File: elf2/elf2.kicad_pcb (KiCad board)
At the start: 4 copper layers, 49.8 x 41.9 mm, 44 parts, among them J1 USB_B, J2 USB_Blaster, J3 JTAGEN, J4 PMOD_I2C, J5 PMOD_6P, J6 PMOD_6P2, J7 SWD, J8 ADC_LVDS, SW1 RESET, U1 EF2M45LG48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

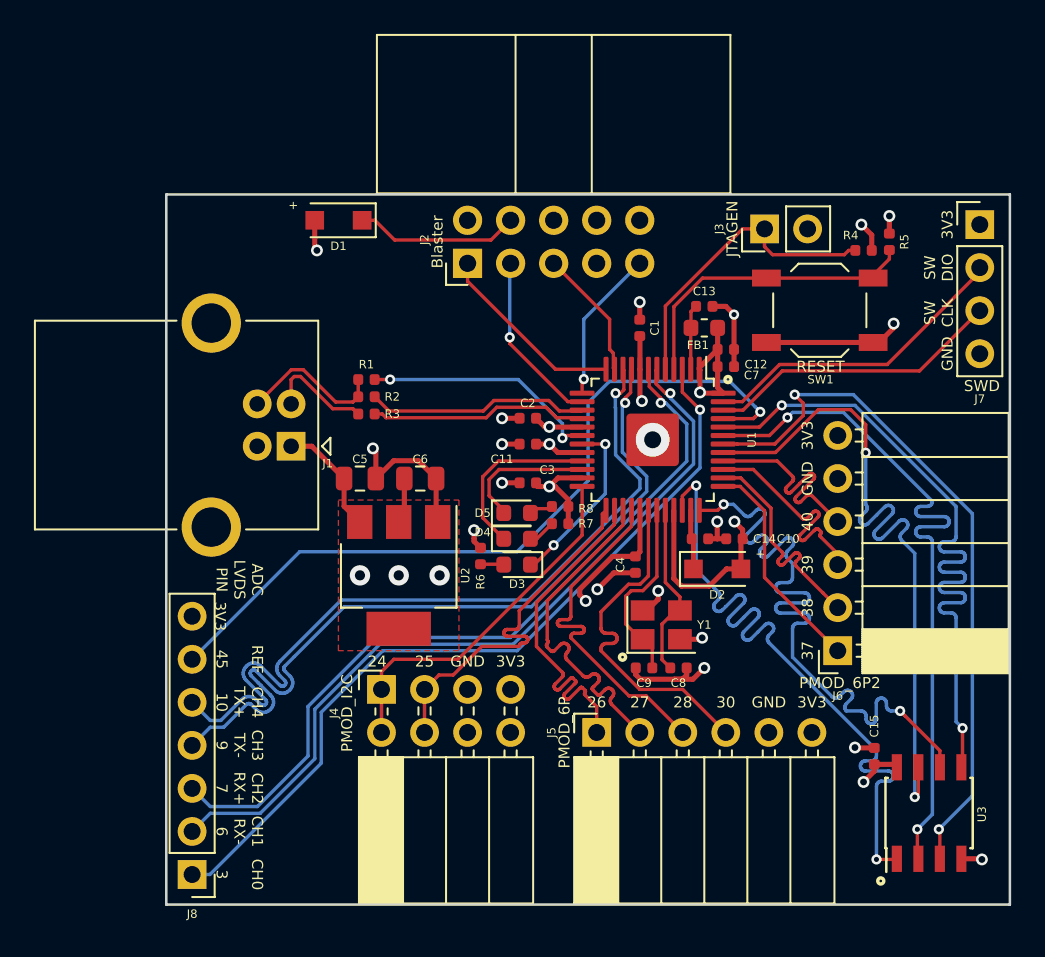
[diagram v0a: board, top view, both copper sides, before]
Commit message: update elf2 to v2
Signed-off-by: Icenowy Zheng <icenowy@aosc.io>
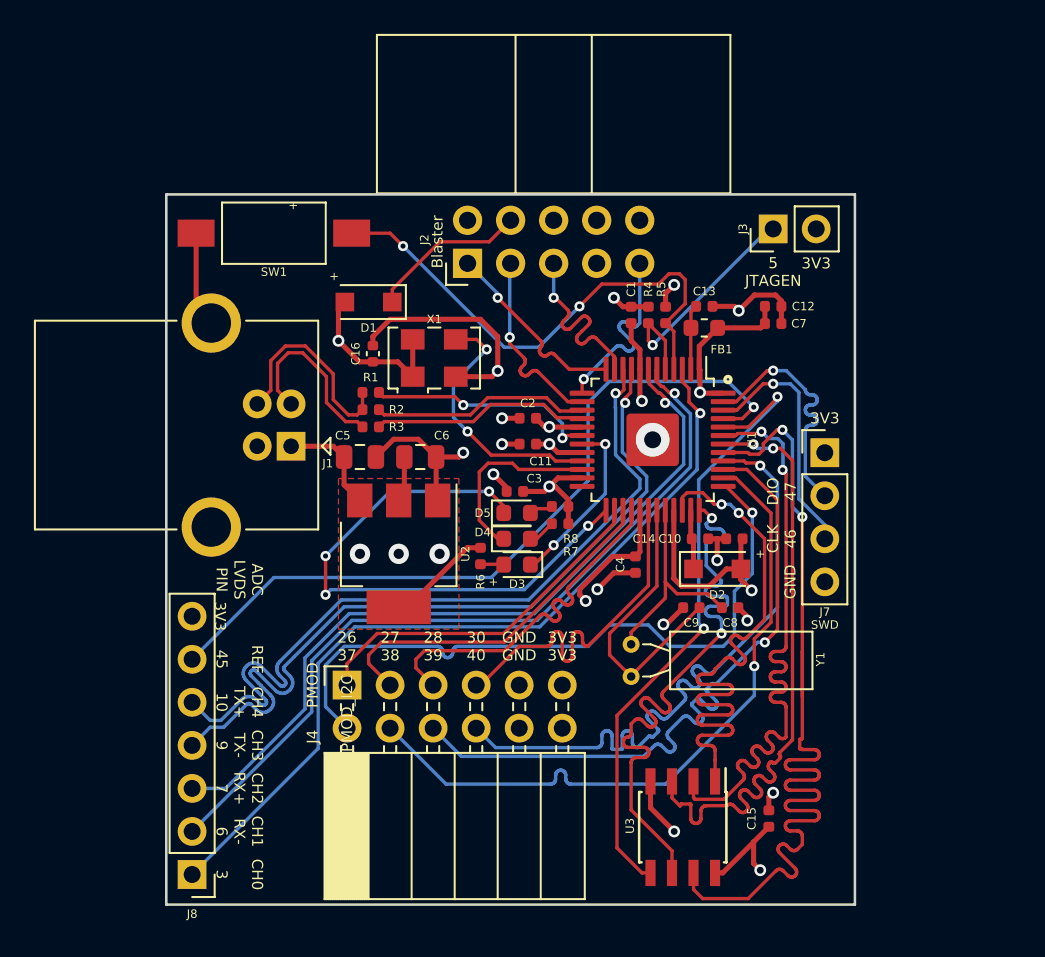
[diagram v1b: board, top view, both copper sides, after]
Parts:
- removed J5: PMOD_6P, Connector_PinSocket_2.54mm:PinSocket_1x06_P2.54mm_Horizontal
- removed J6: PMOD_6P2, Connector_PinSocket_2.54mm:PinSocket_1x06_P2.54mm_Horizontal
- removed the REF** at (117.7, 85.3)
- added C16: 0.1uF, Capacitor_SMD:C_0402_1005Metric, F.Cu at (115.3, 57.4)
- added REF**: KiCad-Logo2_5mm_SilkScreen, Symbol:KiCad-Logo2_5mm_SilkScreen, B.Cu at (112.8, 85.6)
- added X1: 24MHz, Oscillator:Oscillator_SMD_EuroQuartz_XO53-4Pin_5.0x3.2mm, F.Cu at (118.9, 57.7)
- J4: value PMOD_I2C -> PMOD; footprint Connector_PinSocket_2.54mm:PinSocket_2x04_P2.54mm_Horizontal -> Connector_PinSocket_2.54mm:PinSocket_2x06_P2.54mm_Horizontal
- SW1: footprint Button_Switch_SMD:SW_SPST_TL3342 -> Button_Switch_SMD:SW_SPST_FSMSM
- Y1: value 25MHz 12pF -> 32768; footprint Crystal:Crystal_SMD_3225-4Pin_3.2x2.5mm -> Crystal:Crystal_C38-LF_D3.0mm_L8.0mm_Horizontal
- moved SW1 32.5 mm to (109.5, 50.3), turned to 180 degrees
- moved J7 16.3 mm to (142.0, 63.2)
- moved U3 14.6 mm to (133.6, 85.3), turned to 180 degrees
- moved R5 13.9 mm to (132.6, 55.1)
- moved REF** 13.5 mm to (138.4, 79.5)
- moved R4 13.3 mm to (131.6, 55.1), turned to 90 degrees
- moved C15 7.23 mm to (138.7, 84.8)
- moved D1 5.14 mm to (115.1, 54.4)
- moved C8 4.68 mm to (136.4, 72.4)
- moved C9 4.52 mm to (134.1, 72.4)
- moved C12 3.78 mm to (138.9, 54.6)
- moved C7 3.78 mm to (138.9, 55.6)
- moved Y1 3.53 mm to (130.6, 76.5), turned to 90 degrees
- moved J4 2.05 mm to (113.8, 77.0)
- moved C5 1.27 mm to (114.6, 63.5)
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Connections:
- J2 pad 6: Net-(J2-Pad6) -> (no net)
- J2 pad 7: Net-(J2-Pad7) -> (no net)
- J2 pad 8: Net-(J2-Pad8) -> (no net)
- J4 pad 1: /SCL -> /PMOD_6P_1
- J4 pad 2: /SCL -> /PMOD_6P2_1
- J4 pad 3: /SDA -> /PMOD_6P_2
- J4 pad 4: /SDA -> /PMOD_6P2_2
- J4 pad 5: GND -> /PMOD_6P_3
- J4 pad 6: GND -> /PMOD_6P2_3
- J4 pad 7: +3V3 -> /PMOD_6P_4
- J4 pad 8: +3V3 -> /PMOD_6P2_4
- U1 pad 21: /LED_G -> /CLK
- U1 pad 22: /LED_B -> /LED_G
- U1 pad 24: /SCL -> (no net)
- U1 pad 25: /SDA -> /LED_B
- Y1 pad 2: GND -> Net-(C8-Pad1)
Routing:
- net /PMOD_6P2_1: track 13.1 -> 41.0 mm, vias 0 -> 1
- net /PMOD_6P2_4: track 13.1 -> 41.0 mm, vias 0 -> 1
- net /PMOD_6P2_3: track 13.1 -> 41.0 mm, vias 0 -> 1
- net /PMOD_6P2_2: track 13.1 -> 41.0 mm, vias 0 -> 1
- net /LED_B: track 7.95 -> 33.8 mm, vias 0 -> 4
- net /SCL: track 21.6 -> 0.00 mm
- net /SDA: track 21.6 -> 0.00 mm
- net +3V3: track 53.0 -> 73.2 mm, vias 14 -> 13
- net /QSPI_IO3: track 41.5 -> 58.0 mm
- net /CLK: track 0.00 -> 15.6 mm, vias 0 -> 2
- net /PROGRAMN: track 18.2 -> 30.4 mm, vias 0 -> 2
- net GND: track 43.7 -> 51.7 mm, vias 16 -> 14
- net Net-(C9-Pad1): track 10.5 -> 17.2 mm
- net /PORT_D-: track 6.39 -> 10.7 mm
- net /QSPI_IO2: track 41.5 -> 37.3 mm
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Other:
- board size 49.8 x 41.9 mm -> 40.6 x 41.9 mm
- board text added: "26 37"
- board text added: "27 38"
- board text added: "28 39"
- board text added: "30 40"
- board text added: "3V3 3V3"
- board text added: "5 JTAGEN"
- board text added: "CLK 46"
- board text added: "DIO 47"
- board text added: "GND GND"
- board text added: "PMOD"
- board text removed: "24"
- board text removed: "25"
- board text removed: "26"
- board text removed: "27"
- board text removed: "28"
- board text removed: "30"
- board text removed: "37"
- board text removed: "38"
- board text removed: "39"
- board text removed: "40"
- board text removed: "JTAGEN"
- board text removed: "PMOD_6P"
- board text removed: "PMOD_6P2"
- board text removed: "RESET"
- board text removed: "SW CLK"
- board text removed: "SW DIO"
